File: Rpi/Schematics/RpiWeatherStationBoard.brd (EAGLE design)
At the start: 55.5 x 48.2 mm, 6 parts

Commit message: created gerber files for pcb
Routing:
- net GND: track 134.6 -> 143.6 mm
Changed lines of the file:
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@@
 <?xml version="1.0" encoding="utf-8"?>
 <!DOCTYPE eagle SYSTEM "eagle.dtd">
-<eagle version="6.5.0">
+<eagle version="7.2.0">
 <drawing>
 <settings>
@@
 </class>
 </classes>
-<designrules name="default">
+<designrules name="SeeedStudio_2layer_DRU_no_angle_20140221">
 <description language="de">&lt;b&gt;EAGLE Design Rules&lt;/b&gt;
 &lt;p&gt;
@@
 necessary adjustments and save your customized
 design rules under a new name.</description>
+<description language="zh">&lt;b&gt;Seeed Studio EAGLE Design Rules&lt;/b&gt;
+</description>
 <param name="layerSetup" value="(1*16)"/>
-<param name="mtCopper" value="0.035mm 0.035mm 0.035mm 0.035mm 0.035mm 0.035mm 0.035mm 0.035mm 0.035mm 0.035mm 0.035mm 0.035mm 0.035mm 0.035mm 0.035mm 0.035mm"/>
-<param name="mtIsolate" value="1.5mm 0.15mm 0.2mm 0.15mm 0.2mm 0.15mm 0.2mm 0.15mm 0.2mm 0.15mm 0.2mm 0.15mm 0.2mm 0.15mm 0.2mm"/>
-<param name="mdWireWire" value="8mil"/>
-<param name="mdWirePad" value="8mil"/>
-<param name="mdWireVia" value="8mil"/>
-<param name="mdPadPad" value="8mil"/>
-<param name="mdPadVia" value="8mil"/>
-<param name="mdViaVia" value="8mil"/>
-<param name="mdSmdPad" value="8mil"/>
-<param name="mdSmdVia" value="8mil"/>
-<param name="mdSmdSmd" value="8mil"/>
+<param name="mtCopper" value="0.035mm 0.0175mm 0.035mm 0.035mm 0.035mm 0.035mm 0.035mm 0.035mm 0.035mm 0.035mm 0.035mm 0.035mm 0.035mm 0.035mm 0.0175mm 0.035mm"/>
+<param name="mtIsolate" value="1.5mm 1.1mm 0.2mm 0.15mm 0.2mm 0.15mm 0.2mm 0.15mm 0.2mm 0.15mm 0.2mm 0.15mm 0.2mm 0.15mm 0.2mm"/>
+<param name="mdWireWire" value="6mil"/>
+<param name="mdWirePad" value="6mil"/>
+<param name="mdWireVia" value="6mil"/>
+<param name="mdPadPad" value="6mil"/>
+<param name="mdPadVia" value="6mil"/>
+<param name="mdViaVia" value="6mil"/>
+<param name="mdSmdPad" value="0mil"/>
+<param name="mdSmdVia" value="0mil"/>
+<param name="mdSmdSmd" value="0mil"/>
 <param name="mdViaViaSameLayer" value="8mil"/>
 <param name="mnLayersViaInSmd" value="2"/>
-<param name="mdCopperDimension" value="40mil"/>
-<param name="mdDrill" value="8mil"/>
+<param name="mdCopperDimension" value="10mil"/>
+<param name="mdDrill" value="10mil"/>
 <param name="mdSmdStop" value="0mil"/>
-<param name="msWidth" value="10mil"/>
-<param name="msDrill" value="24mil"/>
-<param name="msMicroVia" value="9.99mm"/>
+<param name="msWidth" value="6mil"/>
+<param name="msDrill" value="12mil"/>
+<param name="msMicroVia" value="12mil"/>
 <param name="msBlindViaRatio" value="0.5"/>
 <param name="rvPadTop" value="0.25"/>
@@
 <param name="rlMinPadBottom" value="10mil"/>
 <param name="rlMaxPadBottom" value="20mil"/>
-<param name="rlMinViaOuter" value="8mil"/>
+<param name="rlMinViaOuter" value="6mil"/>
 <param name="rlMaxViaOuter" value="20mil"/>
-<param name="rlMinViaInner" value="8mil"/>
+<param name="rlMinViaInner" value="6mil"/>
 <param name="rlMaxViaInner" value="20mil"/>
 <param name="rlMinMicroViaOuter" value="4mil"/>
@@
 <param name="psTop" value="-1"/>
 <param name="psBottom" value="-1"/>
-<param name="psFirst" value="-1"/>
+<param name="psFirst" value="0"/>
 <param name="psElongationLong" value="100"/>
 <param name="psElongationOffset" value="100"/>
 <param name="mvStopFrame" value="1"/>
 <param name="mvCreamFrame" value="0"/>
-<param name="mlMinStopFrame" value="4mil"/>
-<param name="mlMaxStopFrame" value="4mil"/>
+<param name="mlMinStopFrame" value="2mil"/>
+<param name="mlMaxStopFrame" value="2mil"/>
 <param name="mlMinCreamFrame" value="0mil"/>
 <param name="mlMaxCreamFrame" value="0mil"/>
-<param name="mlViaStopLimit" value="0mil"/>
+<param name="mlViaStopLimit" value="100mil"/>
 <param name="srRoundness" value="0"/>
 <param name="srMinRoundness" value="0mil"/>
@@
 <param name="checkAngle" value="0"/>
 <param name="checkFont" value="1"/>
-<param name="checkRestrict" value="1"/>
+<param name="checkRestrict" value="0"/>
 <param name="useDiameter" value="13"/>
 <param name="maxErrors" value="50"/>
@@
 <pass name="Default">
 <param name="RoutingGrid" value="50mil"/>
+<param name="AutoGrid" value="1"/>
+<param name="Efforts" value="0"/>
+<param name="TopRouterVariant" value="1"/>
 <param name="tpViaShape" value="round"/>
 <param name="PrefDir.1" value="|"/>
@@
 <signals>
 <signal name="GND">
-<contactref element="JP8" pad="6"/>
 <contactref element="JP8" pad="9"/>
 <contactref element="JP8" pad="14"/>
@@
 <contactref element="C3V" pad="2"/>
 <contactref element="C5V" pad="2"/>
-<contactref element="U1" pad="GND"/>
 <wire x1="91.44" y1="24.13" x2="92.71" y2="24.13" width="0.254" layer="1"/>
 <contactref element="SV2" pad="3"/>
@@
 <wire x1="77.47" y1="8.89" x2="77.47" y2="7.62" width="0.254" layer="1"/>
 <wire x1="77.47" y1="8.89" x2="90.17" y2="8.89" width="0.254" layer="1"/>
-<wire x1="66.04" y1="33.02" x2="64.77" y2="34.29" width="0.254" layer="1"/>
-<wire x1="66.04" y1="26.67" x2="66.04" y2="33.02" width="0.254" layer="1"/>
+<wire x1="66.04" y1="26.67" x2="66.04" y2="32.9184" width="0.254" layer="1"/>
+<wire x1="66.04" y1="32.9184" x2="66.04" y2="33.02" width="0.254" layer="1"/>
 <wire x1="67.31" y1="25.4" x2="66.04" y2="26.67" width="0.254" layer="1"/>
 <wire x1="91.44" y1="25.4" x2="88.9" y2="25.4" width="0.254" layer="1"/>
 <wire x1="88.9" y1="25.4" x2="81.28" y2="25.4" width="0.254" layer="1"/>
-<wire x1="81.28" y1="25.4" x2="67.31" y2="25.4" width="0.254" layer="1"/>
+<wire x1="67.31" y1="25.4" x2="81.28" y2="25.4" width="0.254" layer="1"/>
 <wire x1="91.44" y1="24.13" x2="91.44" y2="25.4" width="0.254" layer="1"/>
-<wire x1="55.88" y1="20.32" x2="63.5" y2="12.7" width="0.254" layer="1"/>
-<wire x1="55.88" y1="35.56" x2="55.88" y2="20.32" width="0.254" layer="1"/>
-<wire x1="58.42" y1="35.56" x2="55.88" y2="35.56" width="0.254" layer="1"/>
-<wire x1="58.42" y1="33.02" x2="58.42" y2="35.56" width="0.254" layer="1"/>
-<wire x1="64.77" y1="33.02" x2="58.42" y2="33.02" width="0.254" layer="1"/>
-<wire x1="64.77" y1="34.29" x2="64.77" y2="33.02" width="0.254" layer="1"/>
+<wire x1="55.88" y1="20.32" x2="55.9308" y2="20.2692" width="0.254" layer="1"/>
+<wire x1="55.9308" y1="20.2692" x2="63.5" y2="12.7" width="0.254" layer="1"/>
 <wire x1="93.98" y1="17.78" x2="92.71" y2="16.51" width="0.254" layer="1"/>
 <wire x1="93.98" y1="22.86" x2="93.98" y2="17.78" width="0.254" layer="1"/>
@@
 <wire x1="88.9" y1="27.94" x2="90.17" y2="29.21" width="0.254" layer="1"/>
 <wire x1="88.9" y1="25.4" x2="88.9" y2="27.94" width="0.254" layer="1"/>
-<wire x1="91.44" y1="33.02" x2="92.71" y2="34.29" width="0.254" layer="1"/>
 <wire x1="91.44" y1="25.4" x2="91.44" y2="33.02" width="0.254" layer="1"/>
 <wire x1="81.28" y1="13.97" x2="77.47" y2="13.97" width="0.254" layer="1"/>
 <wire x1="81.28" y1="25.4" x2="81.28" y2="13.97" width="0.254" layer="1"/>
+<wire x1="56.007" y1="34.7472" x2="56.007" y2="20.3454" width="0.254" layer="1"/>
+<wire x1="56.6928" y1="35.433" x2="56.007" y2="34.7472" width="0.254" layer="1"/>
+<wire x1="57.6072" y1="35.433" x2="56.6928" y2="35.433" width="0.254" layer="1"/>
+<wire x1="58.5216" y1="34.5186" x2="57.6072" y2="35.433" width="0.254" layer="1"/>
+<wire x1="58.5216" y1="34.0614" x2="58.5216" y2="34.5186" width="0.254" layer="1"/>
+<wire x1="59.6646" y1="32.9184" x2="58.5216" y2="34.0614" width="0.254" layer="1"/>
+<wire x1="66.04" y1="32.9184" x2="64.9224" y2="32.9184" width="0.254" layer="1"/>
+<wire x1="64.9224" y1="32.9184" x2="59.6646" y2="32.9184" width="0.254" layer="1"/>
+<wire x1="56.007" y1="20.3454" x2="55.9308" y2="20.2692" width="0.254" layer="1"/>
+<wire x1="66.0654" y1="32.9184" x2="66.04" y2="32.9184" width="0.254" layer="1"/>
+<contactref element="JP8" pad="6"/>
+<contactref element="U1" pad="GND"/>
+<wire x1="64.9224" y1="32.9184" x2="64.9224" y2="34.29" width="0.254" layer="1"/>
+<wire x1="64.9224" y1="34.29" x2="64.77" y2="34.29" width="0.254" layer="1"/>
+<wire x1="93.726" y1="24.2316" x2="92.8116" y2="24.2316" width="0.254" layer="1"/>
+<wire x1="94.6404" y1="25.146" x2="93.726" y2="24.2316" width="0.254" layer="1"/>
+<wire x1="94.6404" y1="33.3756" x2="94.6404" y2="25.146" width="0.254" layer="1"/>
+<wire x1="93.726" y1="34.29" x2="94.6404" y2="33.3756" width="0.254" layer="1"/>
+<wire x1="92.71" y1="34.29" x2="93.726" y2="34.29" width="0.254" layer="1"/>
+<wire x1="92.8116" y1="24.2316" x2="92.71" y2="24.13" width="0.254" layer="1"/>
 </signal>
 <signal name="5V">

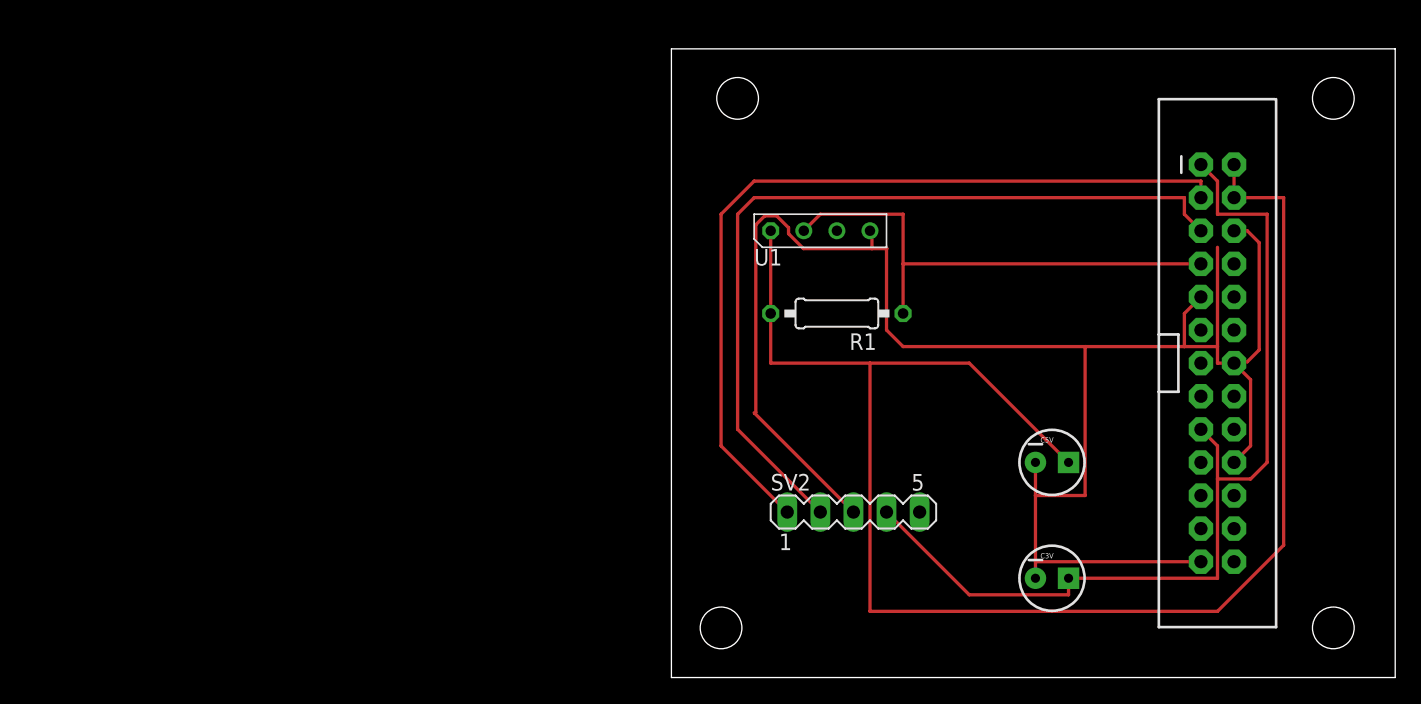
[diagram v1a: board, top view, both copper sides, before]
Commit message: resized board made it 2 layers
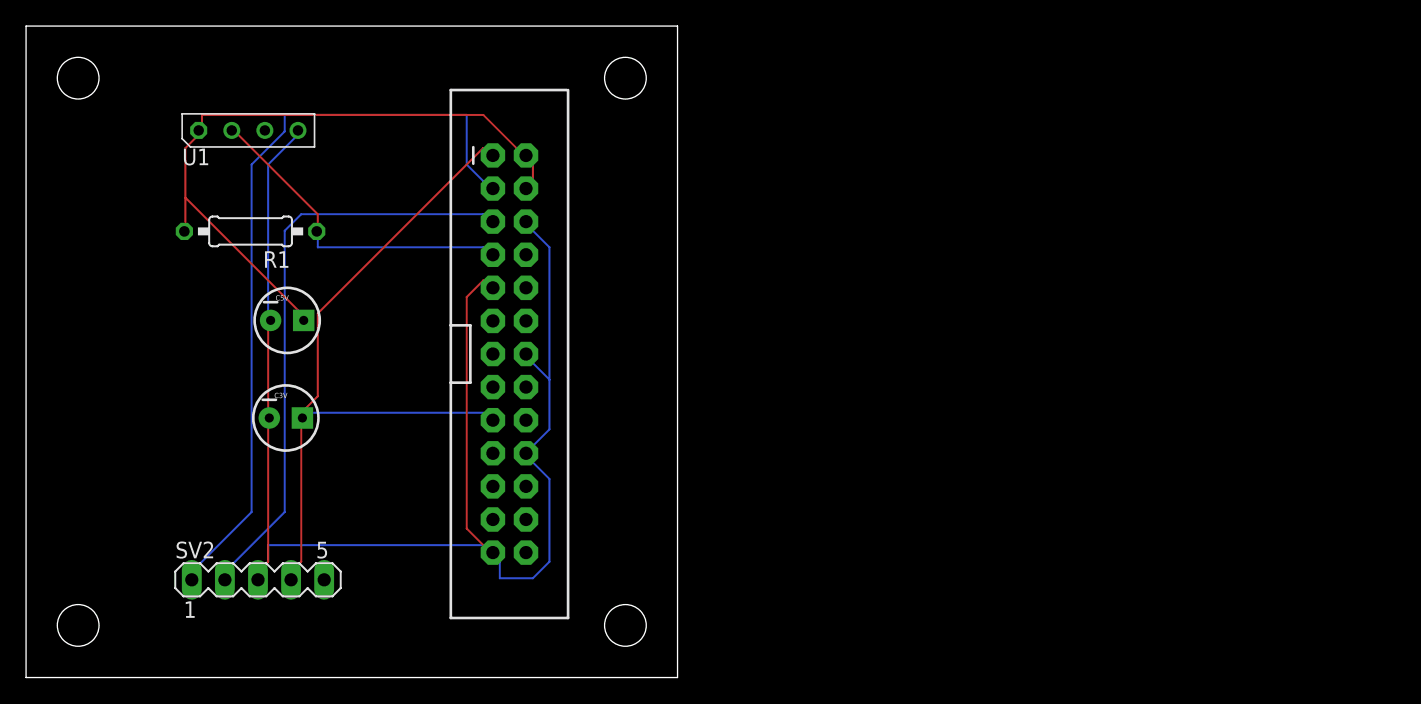
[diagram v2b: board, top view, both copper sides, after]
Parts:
- moved C3V 60.1 mm to (19.9, 19.9)
- moved C5V 59.7 mm to (20.0, 27.4)
- moved JP8 54.3 mm to (37.1, 24.8)
- moved SV2 46.0 mm to (17.8, 7.50)
- moved R1 45.4 mm to (17.2, 34.2)
- moved U1 44.6 mm to (17.1, 42.0)
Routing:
- net 5V: track 122.1 -> 52.0 mm
- net GND: track 143.6 -> 118.8 mm
- net N$3: track 63.4 -> 46.0 mm
- net 3.3V: track 72.8 -> 56.5 mm
- net N$2: track 38.6 -> 25.6 mm
- net N$1: track 64.1 -> 59.7 mm
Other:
- board size 55.5 x 48.2 mm -> 50 x 50 mm
